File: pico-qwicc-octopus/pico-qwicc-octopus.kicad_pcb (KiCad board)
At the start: 2 copper layers, 61 x 61 mm, 1 part

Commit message: Early draft to get an idea of how it will look.
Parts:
- added REF**: CONN4_BM04B-SRSS_JST, Ivan Hawkes:CONN4_BM04B-SRSS_JST, F.Cu at (40.6, 53.3)
- added REF**: CONN4_BM04B-SRSS_JST, Ivan Hawkes:CONN4_BM04B-SRSS_JST, F.Cu at (40.6, 33.0)
- added REF**: CONN4_BM04B-SRSS_JST, Ivan Hawkes:CONN4_BM04B-SRSS_JST, F.Cu at (88.9, 63.5)
- added REF**: CONN4_BM04B-SRSS_JST, Ivan Hawkes:CONN4_BM04B-SRSS_JST, F.Cu at (88.9, 43.2)
- added REF**: CONN4_BM04B-SRSS_JST, Ivan Hawkes:CONN4_BM04B-SRSS_JST, F.Cu at (40.6, 63.5)
- added REF**: CONN4_BM04B-SRSS_JST, Ivan Hawkes:CONN4_BM04B-SRSS_JST, F.Cu at (88.9, 53.3)
- added REF**: CONN4_BM04B-SRSS_JST, Ivan Hawkes:CONN4_BM04B-SRSS_JST, F.Cu at (40.6, 43.4)
- added REF**: CONN4_BM04B-SRSS_JST, Ivan Hawkes:CONN4_BM04B-SRSS_JST, F.Cu at (88.9, 33.0)

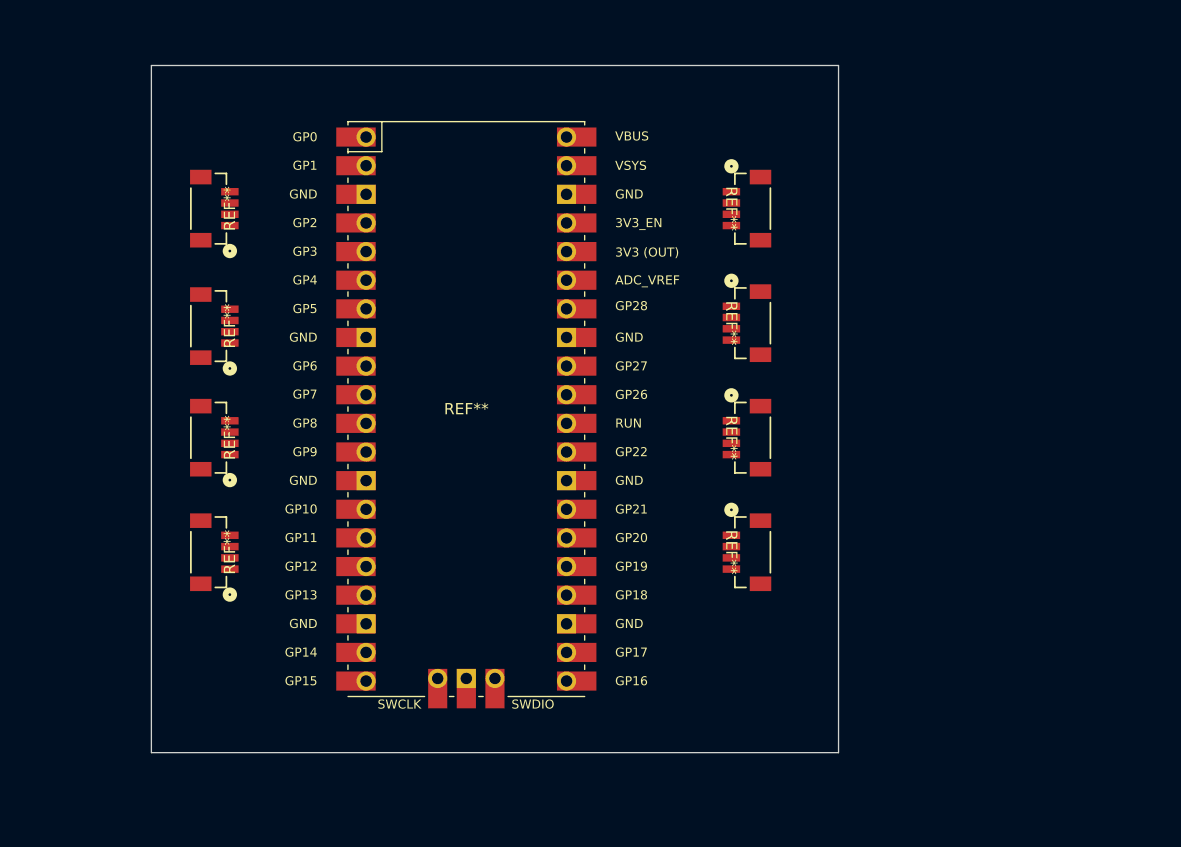
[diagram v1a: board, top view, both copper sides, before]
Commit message: Starting to add connections. Need to make new symbol for the Pico and a footprint.
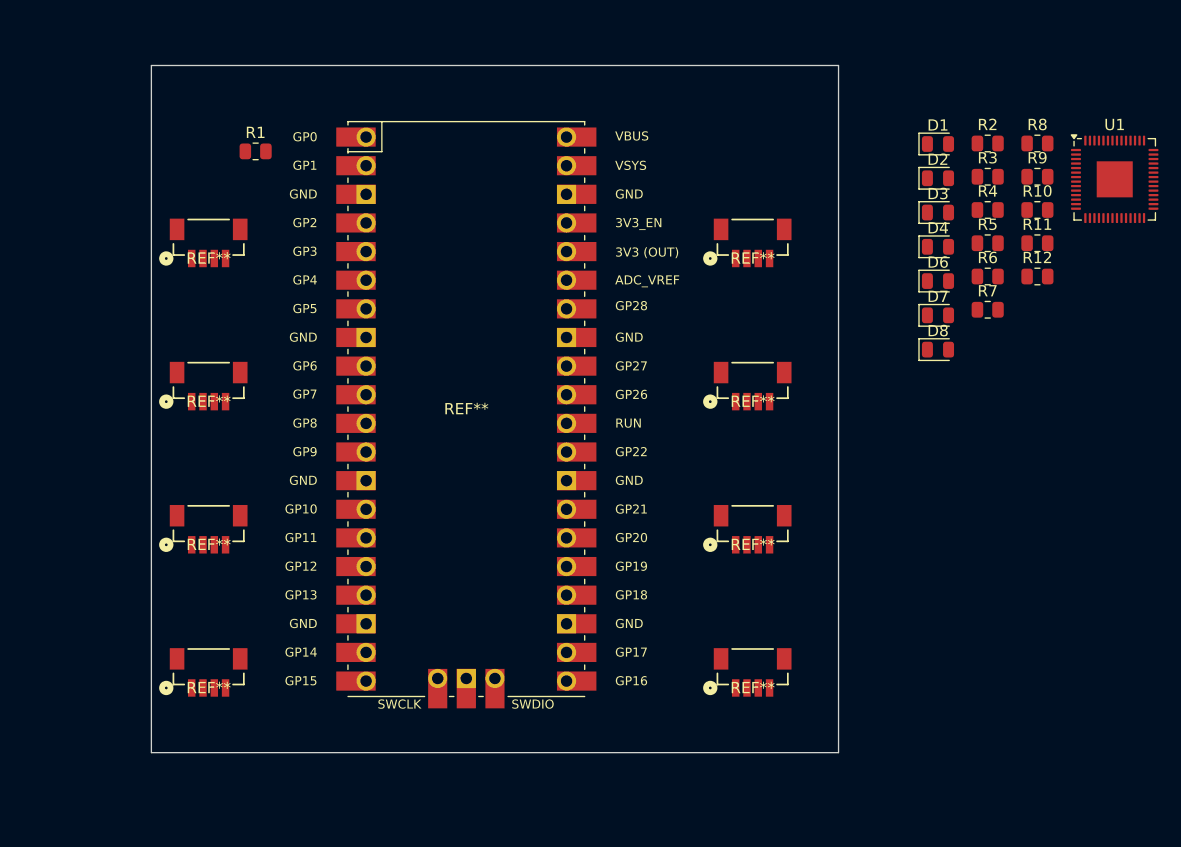
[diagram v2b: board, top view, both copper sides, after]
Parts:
- added D1: LED, LED_SMD:LED_0805_2012Metric, F.Cu at (105.3, 27.3)
- added D2: LED, LED_SMD:LED_0805_2012Metric, F.Cu at (105.3, 30.3)
- added D3: LED, LED_SMD:LED_0805_2012Metric, F.Cu at (105.3, 33.4)
- added D4: LED, LED_SMD:LED_0805_2012Metric, F.Cu at (105.3, 36.4)
- added D6: LED, LED_SMD:LED_0805_2012Metric, F.Cu at (105.3, 39.4)
- added D7: LED, LED_SMD:LED_0805_2012Metric, F.Cu at (105.3, 42.5)
- added D8: LED, LED_SMD:LED_0805_2012Metric, F.Cu at (105.3, 45.5)
- added R1: 100, Resistor_SMD:R_0805_2012Metric, F.Cu at (44.8, 27.9)
- added R10: 220, Resistor_SMD:R_0805_2012Metric, F.Cu at (114.2, 33.1)
- added R11: 220, Resistor_SMD:R_0805_2012Metric, F.Cu at (114.2, 36.1)
- added R12: 220, Resistor_SMD:R_0805_2012Metric, F.Cu at (114.2, 39.0)
- added R2: 100, Resistor_SMD:R_0805_2012Metric, F.Cu at (109.8, 27.2)
- added R3: 250, Resistor_SMD:R_0805_2012Metric, F.Cu at (109.8, 30.2)
- added R4: 250, Resistor_SMD:R_0805_2012Metric, F.Cu at (109.8, 33.1)
- added R5: 220, Resistor_SMD:R_0805_2012Metric, F.Cu at (109.8, 36.1)
- added R6: 220, Resistor_SMD:R_0805_2012Metric, F.Cu at (109.8, 39.0)
- added R7: 220, Resistor_SMD:R_0805_2012Metric, F.Cu at (109.8, 42.0)
- added R8: 220, Resistor_SMD:R_0805_2012Metric, F.Cu at (114.2, 27.2)
- added R9: 220, Resistor_SMD:R_0805_2012Metric, F.Cu at (114.2, 30.2)
- added U1: RP2040, Package_DFN_QFN:QFN-56-1EP_7x7mm_P0.4mm_EP3.2x3.2mm, F.Cu at (121.0, 30.4)
- moved REF** 10.2 mm to (88.9, 73.7), turned to 0 degrees
- moved REF** 10.2 mm to (40.6, 73.7), turned to 0 degrees
- moved REF** 7.62 mm to (40.6, 61.0), turned to 0 degrees
- moved REF** 7.62 mm to (88.9, 61.0), turned to 0 degrees
- moved REF** 5.08 mm to (88.9, 48.3), turned to 0 degrees
- moved REF** 4.82 mm to (40.6, 48.3), turned to 0 degrees
- moved REF** 2.54 mm to (40.6, 35.6), turned to 0 degrees
- moved REF** 2.54 mm to (88.9, 35.6), turned to 0 degrees

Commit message: Trying to get just the basics working.
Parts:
- removed D1, D2, D3, D4, D6, D7, D8: LED, LED_SMD:LED_0805_2012Metric
- removed R10, R11, R12, R5, R6, R7, R8, R9: 220, Resistor_SMD:R_0805_2012Metric
- removed the REF** at (40.6, 61.0)
- removed the REF** at (40.6, 35.6)
- removed the REF** at (88.9, 73.7)
- removed the REF** at (88.9, 48.3)
- removed the REF** at (40.6, 73.7)
- removed the REF** at (88.9, 61.0)
- removed the REF** at (40.6, 48.3)
- removed the REF** at (88.9, 35.6)
- removed U1: RP2040, Package_DFN_QFN:QFN-56-1EP_7x7mm_P0.4mm_EP3.2x3.2mm
- added J1: B3B-XH-A, Ivan Hawkes:CONN_B3B-XH-A_JST, F.Cu at (37.6, 27.4)
- added J2: BM04B-SRSS-TB, Ivan Hawkes:CONN4_BM04B-SRSS_JST, F.Cu at (36.8, 39.4)
- R3, R4: value 250 -> 100
- moved R4 66.0 mm to (44.3, 41.9)
- moved R3 65.9 mm to (44.5, 39.4)
- moved R2 65.3 mm to (44.6, 32.0)
- moved R1 0.55 mm to (44.6, 27.4)
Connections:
- R1 pad 1: Net-(U1-GPIO0) -> /TX
- R1 pad 2: unconnected-(R1-Pad2) -> Net-(J1-Pad1)
- R2 pad 1: Net-(U1-GPIO1) -> /RX
- R2 pad 2: unconnected-(R2-Pad2) -> Net-(J1-Pad3)
- R3 pad 1: Net-(U1-GPIO2) -> /SDA
- R3 pad 2: +3.3V -> Net-(J2-Pad3)
- R4 pad 1: Net-(U1-GPIO3) -> /SCL
- R4 pad 2: +3.3V -> Net-(J2-Pad4)
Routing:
- net (no net): track 0.00 -> 34.7 mm, vias 0 -> 1
- net Net-(J1-Pad3): track 0.00 -> 5.44 mm
- net Net-(J1-Pad1): track 0.00 -> 5.26 mm
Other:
- board size 61 x 61 mm -> 78.7 x 68.6 mm
- board text added: "RX"
- board text added: "TX"

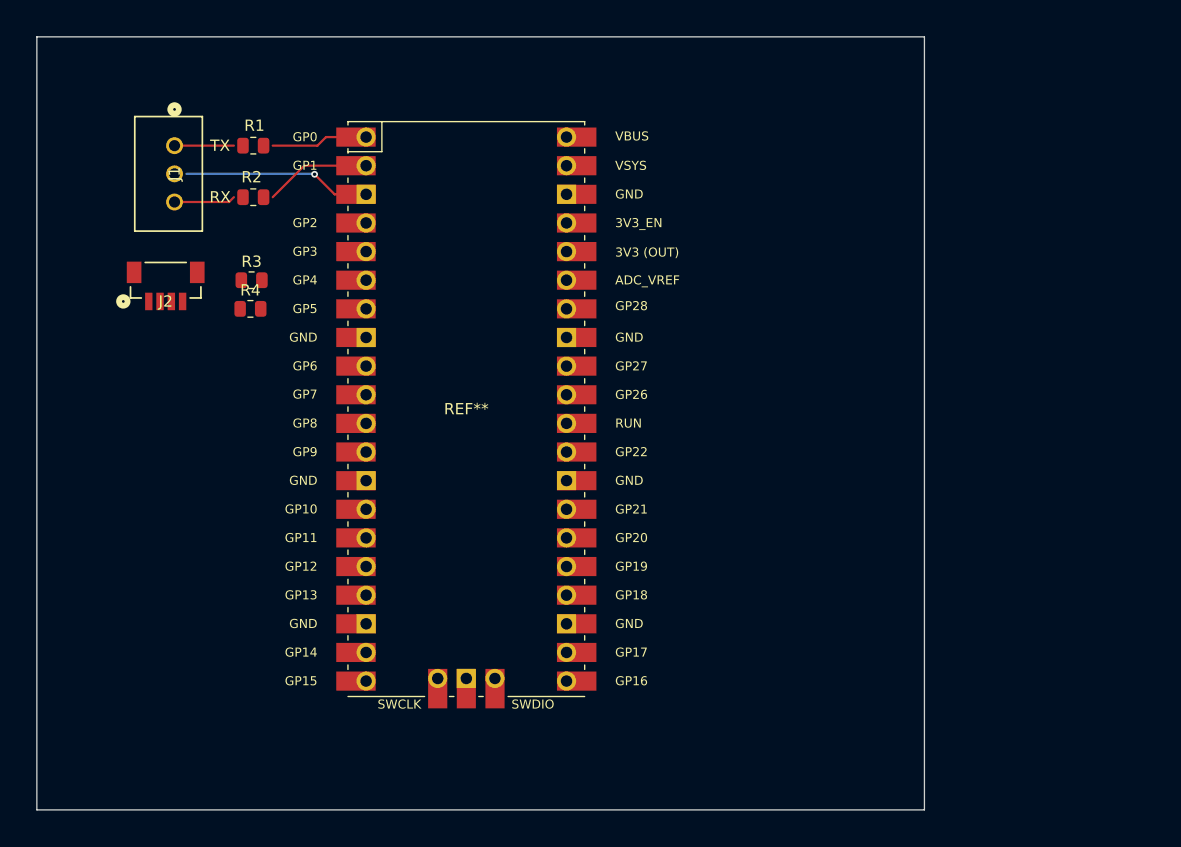
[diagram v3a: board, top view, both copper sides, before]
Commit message: Finally getting the hang of routing. Found out how to stop warnings on ERC tests.
Considering having the board with only a couple of separate I2C connections. It seems they work better when routed through instead of a star configuration.
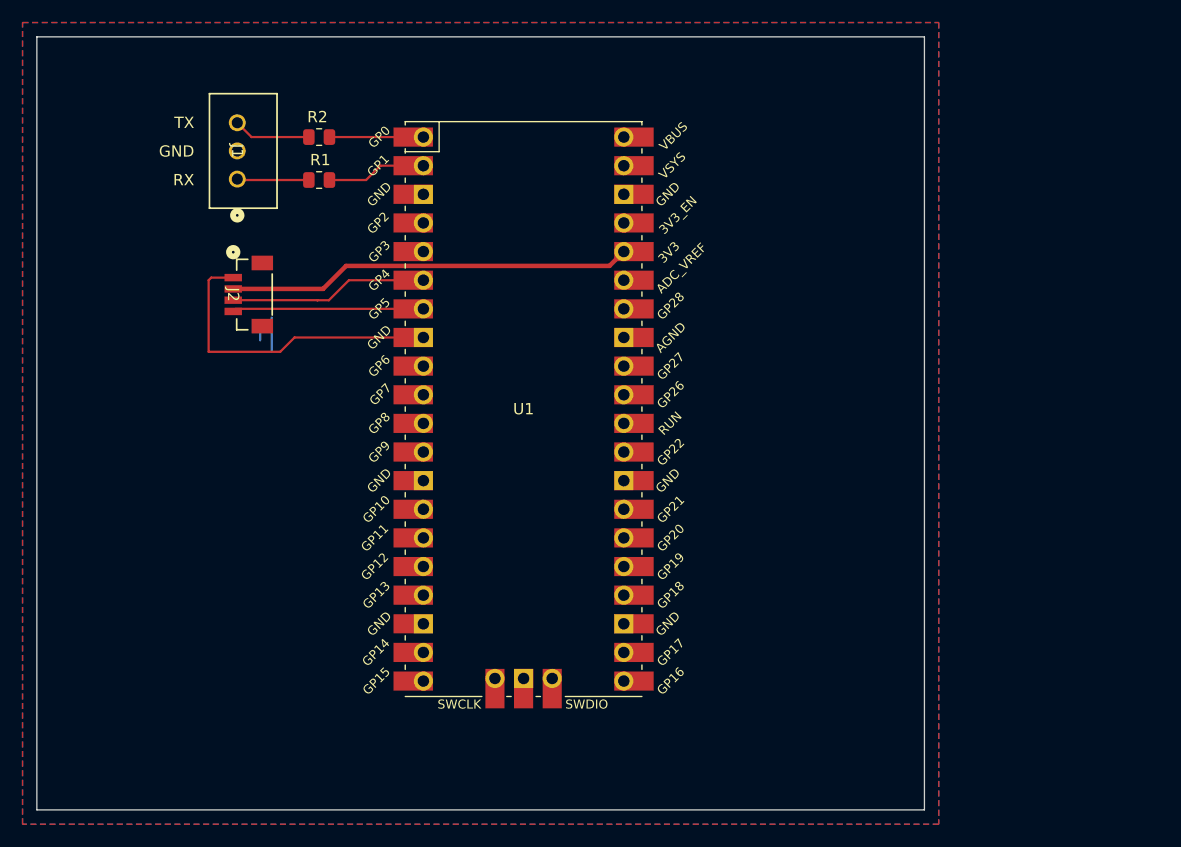
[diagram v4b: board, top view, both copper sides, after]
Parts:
- removed R3, R4: 100, Resistor_SMD:R_0805_2012Metric
- removed REF**: RPi_Pico_SMD_TH, Ivan Hawkes:RPi_Pico_SMD_TH
- added U1: Pico, 00_General:RPi-Pico-SMD-TH, F.Cu at (68.6, 50.8)
- J1: footprint Ivan Hawkes:CONN_B3B-XH-A_JST -> 00_Connectors:JST-B3B-XH-A
- J2: footprint Ivan Hawkes:CONN4_BM04B-SRSS_JST -> 00_Connectors:JST-BM04B-SRSS
- moved J2 7.98 mm to (44.7, 40.6), turned to -90 degrees
- moved R2 7.91 mm to (50.4, 26.7)
- moved R1 6.59 mm to (50.4, 30.5)
- moved J1 6.31 mm to (43.2, 30.4), turned to -90 degrees
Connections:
- J1 pad 1: Net-(J1-Pad1) -> /RX
- J1 pad 3: Net-(J1-Pad3) -> /TX
- J2 pad 3: Net-(J2-Pad3) -> /SDA
- J2 pad 4: Net-(J2-Pad4) -> /SCL
- R1 pad 1: /TX -> /RX
- R1 pad 2: Net-(J1-Pad1) -> /RX
- R2 pad 1: /RX -> /TX
- R2 pad 2: Net-(J1-Pad3) -> /TX
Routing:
- net +3V3: track 0.00 -> 36.0 mm
- net (no net): track 34.7 -> 0.00 mm, vias 1 -> 0
- net GND: track 0.00 -> 28.2 mm
- net /SCL: track 0.00 -> 20.0 mm
- net /SDA: track 0.00 -> 19.4 mm
- net /RX: track 0.00 -> 15.2 mm
- net /TX: track 0.00 -> 15.2 mm
- net Net-(J1-Pad3): track 5.44 -> 0.00 mm
- net Net-(J1-Pad1): track 5.26 -> 0.00 mm
- added copper zone on B.Cu, net GND
- added copper zone on F.Cu, net GND
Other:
- board text added: "GND"
